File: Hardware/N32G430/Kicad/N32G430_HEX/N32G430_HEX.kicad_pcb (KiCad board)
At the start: 2 copper layers, 1 part

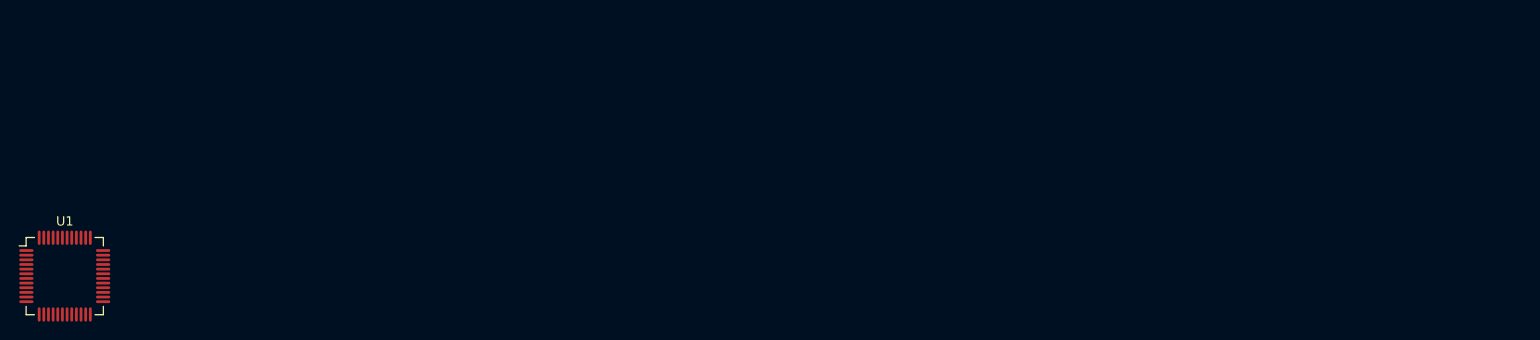
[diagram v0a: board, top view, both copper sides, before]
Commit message: N32G430核心板绘制
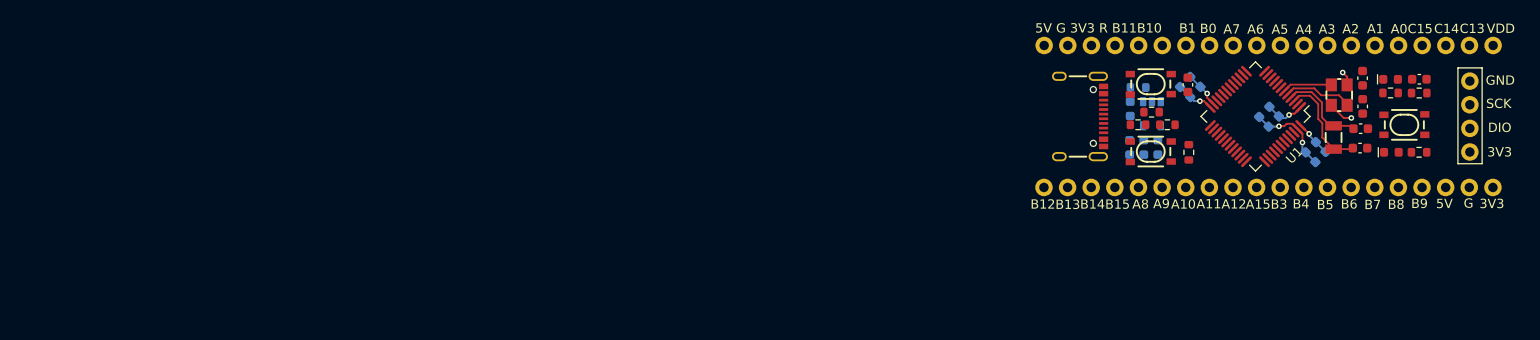
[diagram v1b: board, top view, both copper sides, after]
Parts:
- added C1: 4.7uF, SparkFun-Capacitor:C_0603_1608Metric, B.Cu at (221.1, 34.4)
- added C10: 0.1uF, SparkFun-Capacitor:C_0603_1608Metric, B.Cu at (228.5, 36.5)
- added C11: 0.1uF, SparkFun-Capacitor:C_0603_1608Metric, B.Cu at (229.5, 37.5)
- added C12: 1uF, SparkFun-Capacitor:C_0603_1608Metric, B.Cu at (214.1, 36.2)
- added C13: 1uF, SparkFun-Capacitor:C_0603_1608Metric, B.Cu at (217.1, 40.3)
- added C14: 100nF, SparkFun-Capacitor:C_0603_1608Metric, B.Cu at (215.6, 40.3)
- added C15: 100nF, SparkFun-Capacitor:C_0603_1608Metric, B.Cu at (214.1, 40.3)
- added C16: 1uF, SparkFun-Capacitor:C_0603_1608Metric, F.Cu at (245.2, 33.0)
- added C2: 0.1uF, SparkFun-Capacitor:C_0603_1608Metric, B.Cu at (220.0, 33.3)
- added C3: 0.1uF, SparkFun-Capacitor:C_0603_1608Metric, B.Cu at (233.5, 40.3)
- added C4: 1uF, SparkFun-Capacitor:C_0603_1608Metric, B.Cu at (234.6, 41.4)
- added C5: 0.1uF, SparkFun-Capacitor:C_0603_1608Metric, F.Cu at (220.3, 33.6)
- added C6: 9pF, SparkFun-Capacitor:C_0603_1608Metric, F.Cu at (238.8, 40.4)
- added C7: 9pF, SparkFun-Capacitor:C_0603_1608Metric, F.Cu at (238.9, 38.3)
- added C8: 12pF, SparkFun-Capacitor:C_0603_1608Metric, F.Cu at (239.1, 32.9)
- added C9: 12pF, SparkFun-Capacitor:C_0603_1608Metric, F.Cu at (239.1, 35.9)
- added D1: Red, SparkFun-LED:LED_0603_1608Metric_Red, F.Cu at (242.2, 40.9)
- added D2: Blue, SparkFun-LED:LED_0603_1608Metric_Blue, F.Cu at (242.1, 33.0)
- added J1: USB_C_Receptacle, SparkFun-Connector:USB-C_16, F.Cu at (211.6, 37.0)
- added J2: Conn_01x20, SparkFun-Connector:1x20, F.Cu at (204.9, 29.4)
- added J3: Conn_01x20, SparkFun-Connector:1x20, F.Cu at (253.1, 44.6)
- added J4: Conn_01x04, SparkFun-Connector:1x04, F.Cu at (250.6, 40.8)
- added R1: 5.1k, SparkFun-Resistor:R_0603_1608Metric, B.Cu at (215.0, 33.9)
- added R2: 5.1k, SparkFun-Resistor:R_0603_1608Metric, F.Cu at (216.4, 36.5)
- added R3: 5.1k, SparkFun-Resistor:R_0603_1608Metric, F.Cu at (215.0, 37.9)
- added R4: 10k, SparkFun-Resistor:R_0603_1608Metric, F.Cu at (220.4, 40.9)
- added R5: 1k, SparkFun-Resistor:R_0603_1608Metric, F.Cu at (218.1, 37.9)
- added R6: 5.1k, SparkFun-Resistor:R_0603_1608Metric, F.Cu at (245.2, 34.5)
- added R7: 1k, SparkFun-Resistor:R_0603_1608Metric, F.Cu at (245.2, 40.9)
- added R8: 1k, SparkFun-Resistor:R_0603_1608Metric, F.Cu at (242.1, 34.5)
- added SW1: SMD_4.2x3.2mm_h2.5mm, SparkFun-Switch:Push_SMD_4.2x3.2mm, F.Cu at (216.3, 33.5)
- added SW2: SMD_4.2x3.2mm_h2.5mm, SparkFun-Switch:Push_SMD_4.2x3.2mm, F.Cu at (216.3, 40.8)
- added SW3: SMD_4.2x3.2mm_h2.5mm, SparkFun-Switch:Push_SMD_4.2x3.2mm, F.Cu at (243.6, 37.9)
- added U2: ~, Power_BrookDawn:SGM2019, B.Cu at (215.0, 38.7)
- added Y1: 8MHz, SparkFun-Clock:Crystal_SMD_3.2x2.5mm, F.Cu at (236.6, 34.7)
- added Y2: 32.768kHz, SparkFun-Clock:Crystal_SMD_3.2x1.5mm, F.Cu at (236.0, 39.3)
- moved U1 129.1 mm to (227.6, 37.0), turned to -135 degrees
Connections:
- U1 pad 1: unconnected-(U1-VDD-Pad1) -> VDD
- U1 pad 10: unconnected-(U1-PA0-Pad10) -> /PA0
- U1 pad 11: unconnected-(U1-PA1-Pad11) -> /PA1
- U1 pad 12: unconnected-(U1-PA2-Pad12) -> /PA2
- U1 pad 13: unconnected-(U1-PA3-Pad13) -> /PA3
- U1 pad 14: unconnected-(U1-PA4-Pad14) -> /PA4
- U1 pad 15: unconnected-(U1-PA5-Pad15) -> /PA5
- U1 pad 16: unconnected-(U1-PA6-Pad16) -> /PA6
- U1 pad 17: unconnected-(U1-PA7-Pad17) -> /PA7
- U1 pad 18: unconnected-(U1-PB0-Pad18) -> /PB7
- U1 pad 19: unconnected-(U1-PB1-Pad19) -> /PB0
- U1 pad 2: unconnected-(U1-PC13-TAMPER-RTC-Pad2) -> /PC13
- U1 pad 20: unconnected-(U1-PB2-Pad20) -> /PB1
- U1 pad 21: unconnected-(U1-PB10-Pad21) -> /PB2
- U1 pad 22: unconnected-(U1-PB11-Pad22) -> /PB11
- U1 pad 25: unconnected-(U1-PB12-Pad25) -> /PB12
- U1 pad 26: unconnected-(U1-PB13-Pad26) -> /PB13
- U1 pad 27: unconnected-(U1-PB14-Pad27) -> /PB14
- U1 pad 28: unconnected-(U1-PB15-Pad28) -> /PB15
- U1 pad 29: unconnected-(U1-PA8-Pad29) -> /PA8
- U1 pad 3: unconnected-(U1-PC14-OSC32_IN-Pad3) -> Net-(U1-PC14-OSC32_IN)
- U1 pad 30: unconnected-(U1-PA9-Pad30) -> /PA9
- U1 pad 31: unconnected-(U1-PA10-Pad31) -> /PA10
- U1 pad 32: unconnected-(U1-PA11-Pad32) -> /PA11
- U1 pad 33: unconnected-(U1-PA12-Pad33) -> /PA12
- U1 pad 34: unconnected-(U1-PA13-Pad34) -> DIO
- U1 pad 35: unconnected-(U1-PD12-Pad35) -> /PD12
- U1 pad 36: unconnected-(U1-PD13-Pad36) -> /PD13
- U1 pad 37: unconnected-(U1-PA14-Pad37) -> SCK
- U1 pad 38: unconnected-(U1-PA15-Pad38) -> /PA15
- U1 pad 39: unconnected-(U1-PB3-Pad39) -> /PB3
- U1 pad 4: unconnected-(U1-PC15-OSC32_OUT-Pad4) -> Net-(U1-PC15-OSC32_OUT)
- U1 pad 40: unconnected-(U1-PB4-Pad40) -> /PB4
- U1 pad 41: unconnected-(U1-PB5-Pad41) -> /PB5
- U1 pad 42: unconnected-(U1-PB6-Pad42) -> /PB6
- U1 pad 43: unconnected-(U1-PB7-Pad43) -> /PB7
- U1 pad 44: unconnected-(U1-PD0-BOOT0-Pad44) -> /BOOT0
- U1 pad 45: unconnected-(U1-PB8-Pad45) -> /PB8
- U1 pad 46: unconnected-(U1-PB9-Pad46) -> /PB9
- U1 pad 5: unconnected-(U1-PD14-OSC_IN-Pad5) -> Net-(U1-PD14-OSC_IN)
- U1 pad 6: unconnected-(U1-PD15-OSC_OUT-Pad6) -> Net-(U1-PD15-OSC_OUT)
- U1 pad 7: unconnected-(U1-NRST-Pad7) -> /NRST
- U1 pad 8: unconnected-(U1-VSSA-Pad8) -> VSS
- U1 pad 9: unconnected-(U1-VDDA-Pad9) -> VDD
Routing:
- net VSS: track 0.00 -> 17.8 mm, vias 0 -> 5
- net VDD: track 0.00 -> 12.0 mm, vias 0 -> 3
- net Net-(U1-PC14-OSC32_IN): track 0.00 -> 10.8 mm
- net Net-(U1-PC15-OSC32_OUT): track 0.00 -> 9.88 mm
- net Net-(U1-PD14-OSC_IN): track 0.00 -> 7.61 mm
- net Net-(U1-PD15-OSC_OUT): track 0.00 -> 5.35 mm
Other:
- board text added: "3V3"
- board text added: "5V"
- board text added: "5V G 3V3 R B11B10"
- board text added: "A0"
- board text added: "A1"
- board text added: "A10"
- board text added: "A11"
- board text added: "A12"
- board text added: "A15"
- board text added: "A2"
- board text added: "A3"
- board text added: "A4"
- board text added: "A5"
- board text added: "A6"
- board text added: "A7"
- board text added: "A8"
- board text added: "A9"
- board text added: "B0"
- board text added: "B1"
- board text added: "B12"
- board text added: "B13"
- board text added: "B14"
- board text added: "B15"
- board text added: "B3"
- board text added: "B4"
- board text added: "B5"
- board text added: "B6"
- board text added: "B7"
- board text added: "B8"
- board text added: "B9"
- board text added: "C13"
- board text added: "C14"
- board text added: "C15"
- board text added: "DIO"
- board text added: "G"
- board text added: "GND"
- board text added: "SCK"
- board text added: "VDD"
